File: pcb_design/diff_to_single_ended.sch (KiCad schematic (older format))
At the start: 10 parts, among them U14 OPA2376AID

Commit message: Completed some part numbers
Signed-off-by: Marcos Chaparro <mchaparro@paltatech.com>
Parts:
- C65: MFR (none) -> KEMET; MPN (none) -> C0603C101J5GACTU; SPN (none) -> 399-1061-1-ND; SPR (none) -> Digikey
- C72: MFR (none) -> Murata Electronics North America; MPN (none) -> GRM188R71E104KA01D; SPN (none) -> 490-1524-1-ND; SPR (none) -> Digikey

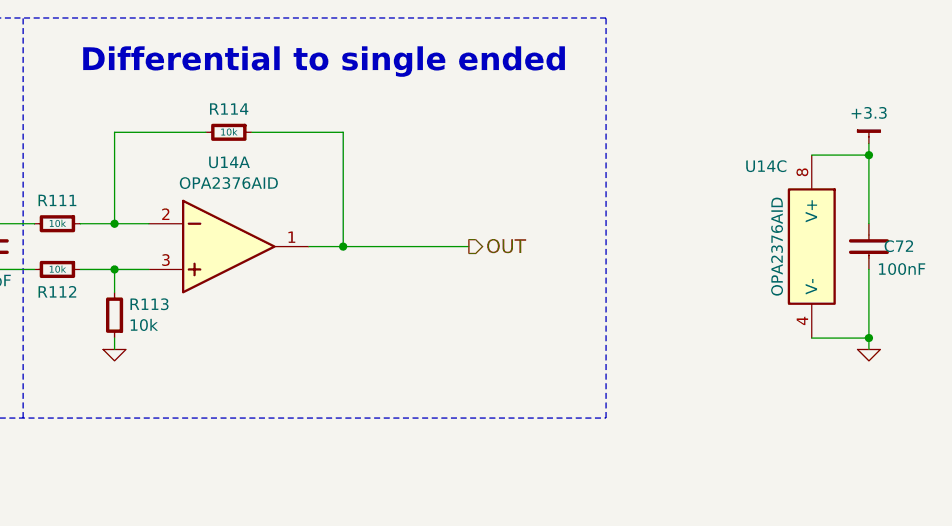
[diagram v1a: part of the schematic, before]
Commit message: Completed part number, manufacturer, etc fields. Simulated analog conditioning
Signed-off-by: Marcos Chaparro <mchaparro@paltatech.com>
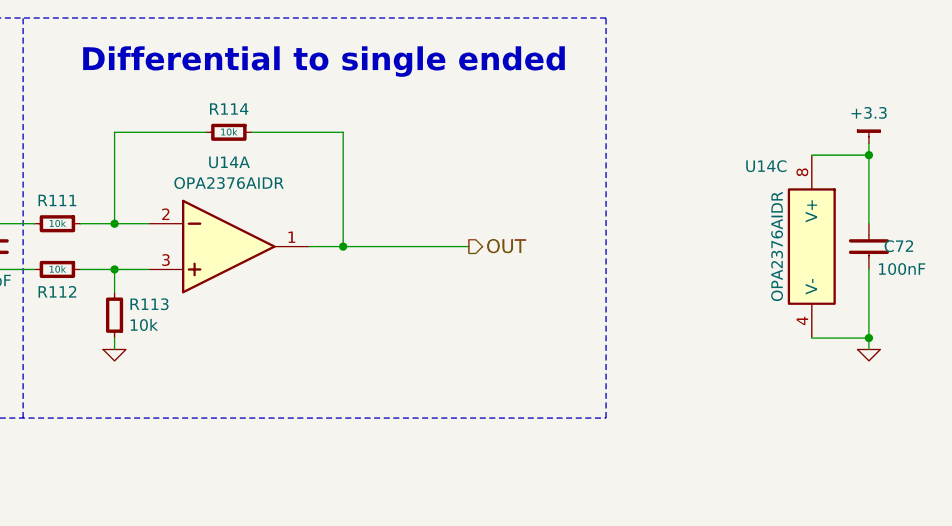
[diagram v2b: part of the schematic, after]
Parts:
- R109, R110: MFR (none) -> Yageo; MPN (none) -> RC0603FR-074K7L; SPN (none) -> 311-4.70KHRCT-ND; SPR (none) -> Digikey
- R111, R112, R113, R114: MFR (none) -> Yageo; MPN (none) -> RC0603FR-0710KL; SPN (none) -> 311-10.0KHRCT-ND; SPR (none) -> Digikey
- R121: MFR (none) -> Yageo; MPN (none) -> RC0603FR-072KL; SPN (none) -> 311-2.00KHRCT-ND; SPR (none) -> Digikey
- U14: value OPA2376AID -> OPA2376AIDR; MFR (none) -> Texas Instruments; MPN (none) -> OPA2376AIDR; SPN (none) -> 296-22564-1-ND; SPR (none) -> Digikey
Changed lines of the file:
@@
 AR Path="/588DB05E/588F2248" Ref="U14" Part="1"
 F 0 "U14" H 6450 4467 50 0000 C CNN
-F 1 "OPA2376AID" H 6450 4376 50 0000 C CNN
+F 1 "OPA2376AIDR" H 6450 4376 50 0000 C CNN
 F 2 "IPC7351-Nominal:SOIC127P600X175-8" H 6400 3850 50 0001 C CNN
-F 3 "" V 6400 4250 60 0000 C CNN
+F 3 "http://www.ti.com/lit/ds/symlink/opa2376.pdf" V 6400 4250 60 0001 C CNN
 F 4 "IC TI OPA2376AID" H 6400 3750 60 0001 C CNN "BOM"
-F 5 "" H 0 0 50 0001 C CNN "MFR"
-F 6 "" H 0 0 50 0001 C CNN "MPN"
-F 7 "" H 0 0 50 0001 C CNN "SPR"
-F 8 "" H 0 0 50 0001 C CNN "SPN"
+F 5 "Texas Instruments" H 0 0 50 0001 C CNN "MFR"
+F 6 "OPA2376AIDR" H 0 0 50 0001 C CNN "MPN"
+F 7 "Digikey" H 0 0 50 0001 C CNN "SPR"
+F 8 "296-22564-1-ND" H 0 0 50 0001 C CNN "SPN"
 F 9 "" H 0 0 50 0001 C CNN "SPURL"
 	1    6400 4100
@@
 F 1 "10k" V 5700 4000 30 0000 C CNN
 F 2 "IPC7351-Nominal:RESC1608X50" H 5700 4000 50 0001 C CNN
-F 3 "" H 5700 4050 60 0000 C CNN
+F 3 "" H 5700 4050 60 0001 C CNN
 F 4 "RES SMD 1k 5% [0603]" H 6450 4550 60 0001 C CNN "BOM"
-F 5 "" H 0 0 50 0001 C CNN "MFR"
-F 6 "" H 0 0 50 0001 C CNN "MPN"
-F 7 "" H 0 0 50 0001 C CNN "SPR"
-F 8 "" H 0 0 50 0001 C CNN "SPN"
+F 5 "Yageo" H 0 0 50 0001 C CNN "MFR"
+F 6 "RC0603FR-0710KL" H 0 0 50 0001 C CNN "MPN"
+F 7 "Digikey" H 0 0 50 0001 C CNN "SPR"
+F 8 "311-10.0KHRCT-ND" H 0 0 50 0001 C CNN "SPN"
 F 9 "" H 0 0 50 0001 C CNN "SPURL"
 	1    5700 4000
@@
 F 1 "10k" V 5700 4200 30 0000 C CNN
 F 2 "IPC7351-Nominal:RESC1608X50" H 5700 4200 50 0001 C CNN
-F 3 "" H 5700 4250 60 0000 C CNN
+F 3 "" H 5700 4250 60 0001 C CNN
 F 4 "RES SMD 1k 5% [0603]" H 6450 4750 60 0001 C CNN "BOM"
-F 5 "" H 0 0 50 0001 C CNN "MFR"
-F 6 "" H 0 0 50 0001 C CNN "MPN"
-F 7 "" H 0 0 50 0001 C CNN "SPR"
-F 8 "" H 0 0 50 0001 C CNN "SPN"
+F 5 "Yageo" H 0 0 50 0001 C CNN "MFR"
+F 6 "RC0603FR-0710KL" H 0 0 50 0001 C CNN "MPN"
+F 7 "Digikey" H 0 0 50 0001 C CNN "SPR"
+F 8 "311-10.0KHRCT-ND" H 0 0 50 0001 C CNN "SPN"
 F 9 "" H 0 0 50 0001 C CNN "SPURL"
 	1    5700 4200
@@
 F 1 "10k" V 6450 3600 30 0000 C CNN
 F 2 "IPC7351-Nominal:RESC1608X50" H 6450 3600 50 0001 C CNN
-F 3 "" H 6450 3650 60 0000 C CNN
+F 3 "" H 6450 3650 60 0001 C CNN
 F 4 "RES SMD 1k 5% [0603]" H 7200 4150 60 0001 C CNN "BOM"
-F 5 "" H 0 0 50 0001 C CNN "MFR"
-F 6 "" H 0 0 50 0001 C CNN "MPN"
-F 7 "" H 0 0 50 0001 C CNN "SPR"
-F 8 "" H 0 0 50 0001 C CNN "SPN"
+F 5 "Yageo" H 0 0 50 0001 C CNN "MFR"
+F 6 "RC0603FR-0710KL" H 0 0 50 0001 C CNN "MPN"
+F 7 "Digikey" H 0 0 50 0001 C CNN "SPR"
+F 8 "311-10.0KHRCT-ND" H 0 0 50 0001 C CNN "SPN"
 F 9 "" H 0 0 50 0001 C CNN "SPURL"
 	1    6450 3600
@@
 F 1 "10k" H 5887 4445 50 0000 R CNN
 F 2 "IPC7351-Nominal:RESC1608X50" H 5950 4400 50 0001 C CNN
-F 3 "" H 5950 4450 60 0000 C CNN
+F 3 "" H 5950 4450 60 0001 C CNN
 F 4 "RES SMD 1k 5% [0603]" H 6700 4950 60 0001 C CNN "BOM"
-F 5 "" H 0 0 50 0001 C CNN "MFR"
-F 6 "" H 0 0 50 0001 C CNN "MPN"
-F 7 "" H 0 0 50 0001 C CNN "SPR"
-F 8 "" H 0 0 50 0001 C CNN "SPN"
+F 5 "Yageo" H 0 0 50 0001 C CNN "MFR"
+F 6 "RC0603FR-0710KL" H 0 0 50 0001 C CNN "MPN"
+F 7 "Digikey" H 0 0 50 0001 C CNN "SPR"
+F 8 "311-10.0KHRCT-ND" H 0 0 50 0001 C CNN "SPN"
 F 9 "" H 0 0 50 0001 C CNN "SPURL"
 	1    5950 4400
@@
 F 1 "4.7k" V 5100 4000 30 0000 C CNN
 F 2 "IPC7351-Nominal:RESC1608X50" H 5100 4000 50 0001 C CNN
-F 3 "" H 5100 4050 60 0000 C CNN
+F 3 "" H 5100 4050 60 0001 C CNN
 F 4 "RES SMD 1k 5% [0603]" H 5850 4550 60 0001 C CNN "BOM"
-F 5 "" H 0 0 50 0001 C CNN "MFR"
-F 6 "" H 0 0 50 0001 C CNN "MPN"
-F 7 "" H 0 0 50 0001 C CNN "SPR"
-F 8 "" H 0 0 50 0001 C CNN "SPN"
+F 5 "Yageo" H 0 0 50 0001 C CNN "MFR"
+F 6 "RC0603FR-074K7L" H 0 0 50 0001 C CNN "MPN"
+F 7 "Digikey" H 0 0 50 0001 C CNN "SPR"
+F 8 "311-4.70KHRCT-ND" H 0 0 50 0001 C CNN "SPN"
 F 9 "" H 0 0 50 0001 C CNN "SPURL"
 	1    5100 4000
@@
 F 1 "4.7k" V 5100 4200 30 0000 C CNN
 F 2 "IPC7351-Nominal:RESC1608X50" H 5100 4200 50 0001 C CNN
-F 3 "" H 5100 4250 60 0000 C CNN
+F 3 "" H 5100 4250 60 0001 C CNN
 F 4 "RES SMD 1k 5% [0603]" H 5850 4750 60 0001 C CNN "BOM"
-F 5 "" H 0 0 50 0001 C CNN "MFR"
-F 6 "" H 0 0 50 0001 C CNN "MPN"
-F 7 "" H 0 0 50 0001 C CNN "SPR"
-F 8 "" H 0 0 50 0001 C CNN "SPN"
+F 5 "Yageo" H 0 0 50 0001 C CNN "MFR"
+F 6 "RC0603FR-074K7L" H 0 0 50 0001 C CNN "MPN"
+F 7 "Digikey" H 0 0 50 0001 C CNN "SPR"
+F 8 "311-4.70KHRCT-ND" H 0 0 50 0001 C CNN "SPN"
 F 9 "" H 0 0 50 0001 C CNN "SPURL"
 	1    5100 4200
@@
 AR Path="/588DB05E/588F2CD6" Ref="U14" Part="3"
 F 0 "U14" H 8800 4450 50 0000 C CNN
-F 1 "OPA2376AID" V 8850 4100 50 0000 C CNN
+F 1 "OPA2376AIDR" V 8850 4100 50 0000 C CNN
 F 2 "IPC7351-Nominal:SOIC127P600X175-8" H 9000 3850 50 0001 C CNN
-F 3 "" V 9000 4250 60 0000 C CNN
+F 3 "http://www.ti.com/lit/ds/symlink/opa2376.pdf" V 9000 4250 60 0001 C CNN
 F 4 "IC TI OPA2376AID" H 9000 3750 60 0001 C CNN "BOM"
-F 5 "" H 0 0 50 0001 C CNN "MFR"
-F 6 "" H 0 0 50 0001 C CNN "MPN"
-F 7 "" H 0 0 50 0001 C CNN "SPR"
-F 8 "" H 0 0 50 0001 C CNN "SPN"
+F 5 "Texas Instruments" H 0 0 50 0001 C CNN "MFR"
+F 6 "OPA2376AIDR" H 0 0 50 0001 C CNN "MPN"
+F 7 "Digikey" H 0 0 50 0001 C CNN "SPR"
+F 8 "296-22564-1-ND" H 0 0 50 0001 C CNN "SPN"
 F 9 "" H 0 0 50 0001 C CNN "SPURL"
 	3    9000 4100
@@
 F 1 "2k" V 4800 4100 30 0000 C CNN
 F 2 "IPC7351-Nominal:RESC1608X50" H 4800 4100 50 0001 C CNN
-F 3 "" H 4800 4150 60 0000 C CNN
+F 3 "" H 4800 4150 60 0001 C CNN
 F 4 "RES SMD 1k 5% [0603]" H 5550 4650 60 0001 C CNN "BOM"
-F 5 "" H 0 0 50 0001 C CNN "MFR"
-F 6 "" H 0 0 50 0001 C CNN "MPN"
-F 7 "" H 0 0 50 0001 C CNN "SPR"
-F 8 "" H 0 0 50 0001 C CNN "SPN"
+F 5 "Yageo" H 0 0 50 0001 C CNN "MFR"
+F 6 "RC0603FR-072KL" H 0 0 50 0001 C CNN "MPN"
+F 7 "Digikey" H 0 0 50 0001 C CNN "SPR"
+F 8 "311-2.00KHRCT-ND" H 0 0 50 0001 C CNN "SPN"
 F 9 "" H 0 0 50 0001 C CNN "SPURL"
 	1    4800 4100

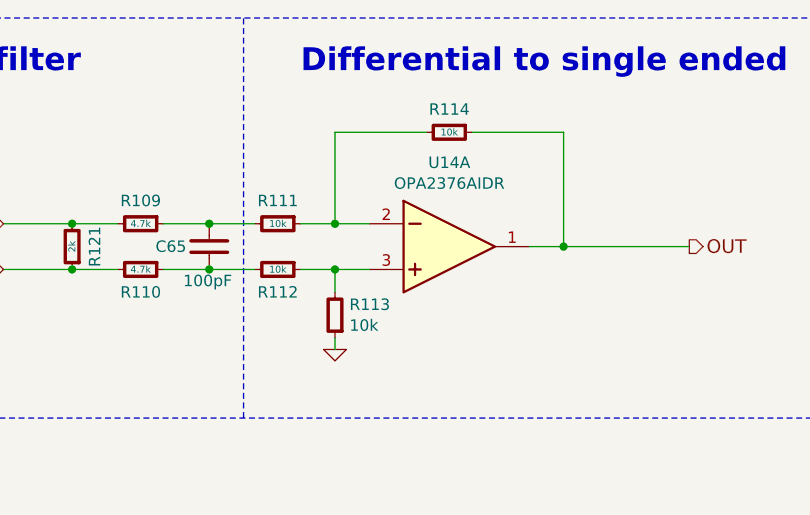
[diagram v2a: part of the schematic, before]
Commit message: Corrected phase current gain. More 3d models
Signed-off-by: Marcos Chaparro <mchaparro@paltatech.com>
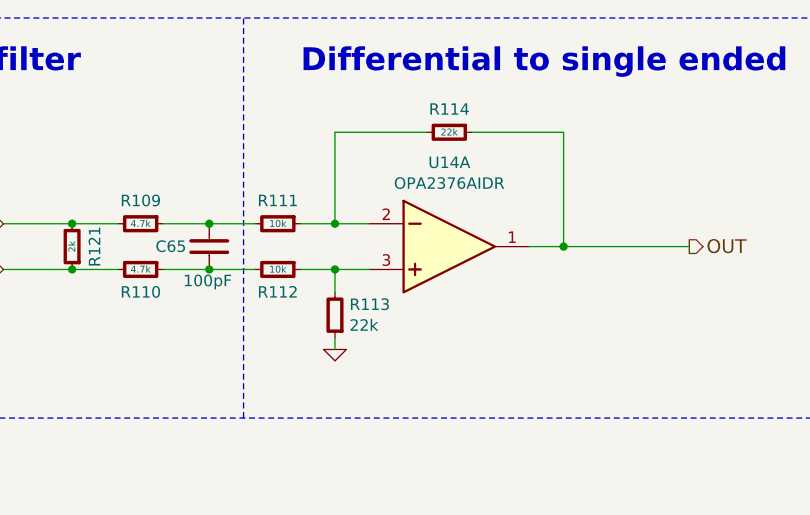
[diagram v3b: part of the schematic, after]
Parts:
- R113, R114: value 10k -> 22k

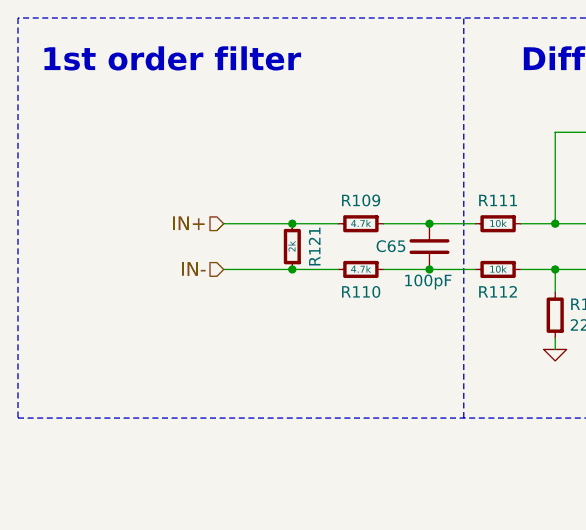
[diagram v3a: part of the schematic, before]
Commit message: Fix inverted diff signals
Signed-off-by: Marcos Chaparro <mchaparro@paltatech.com>
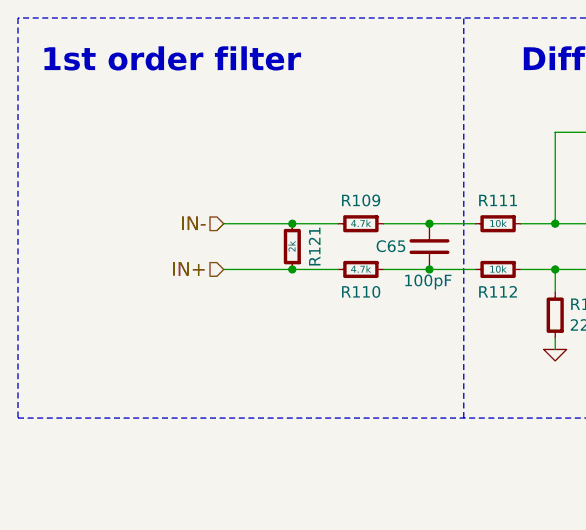
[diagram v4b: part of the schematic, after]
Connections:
- net IN+: now also R110.2, R121.1; no longer R109.2, R121.2
- net IN-: now also R109.2, R121.2; no longer R110.2, R121.1
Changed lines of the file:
@@
 $Descr A4 11693 8268
 encoding utf-8
-Sheet 13 14
+Sheet 11 14
 Title "Differential to single ended"
 Date "2017-02-22"
@@
 EndData
 $EndBitmap
+Text HLabel 4500 4200 0    60   Input ~ 0
+IN+
 Text HLabel 4500 4000 0    60   Input ~ 0
-IN+
-Text HLabel 4500 4200 0    60   Input ~ 0
 IN-
 Text HLabel 7500 4100 2    60   Output ~ 0

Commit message: Added RC filter to FAULT line to prevent noise triggering it
Signed-off-by: Marcos Chaparro <mchaparro@paltatech.com>
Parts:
- C72: BOM CAP MLCC 100pF C0G 50V 5% [0603] -> CAP MLCC 100nF C0G 50V 5% [0603]
- R113, R114: MPN RC0603FR-0710KL -> RC0603FR-0722KL; SPN 311-10.0KHRCT-ND -> 311-22.0KHRCT-ND
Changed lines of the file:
@@
 F 4 "RES SMD 1k 5% [0603]" H 7200 4150 60  0001 C CNN "BOM"
 F 5 "Yageo" H 0   0   50  0001 C CNN "MFR"
-F 6 "RC0603FR-0710KL" H 0   0   50  0001 C CNN "MPN"
+F 6 "RC0603FR-0722KL" H 0   0   50  0001 C CNN "MPN"
 F 7 "Digikey" H 0   0   50  0001 C CNN "SPR"
-F 8 "311-10.0KHRCT-ND" H 0   0   50  0001 C CNN "SPN"
+F 8 "311-22.0KHRCT-ND" H 0   0   50  0001 C CNN "SPN"
 F 9 "" H 0   0   50  0001 C CNN "SPURL"
 	1    6450 3600
@@
 F 4 "RES SMD 1k 5% [0603]" H 6700 4950 60  0001 C CNN "BOM"
 F 5 "Yageo" H 0   0   50  0001 C CNN "MFR"
-F 6 "RC0603FR-0710KL" H 0   0   50  0001 C CNN "MPN"
+F 6 "RC0603FR-0722KL" H 0   0   50  0001 C CNN "MPN"
 F 7 "Digikey" H 0   0   50  0001 C CNN "SPR"
-F 8 "311-10.0KHRCT-ND" H 0   0   50  0001 C CNN "SPN"
+F 8 "311-22.0KHRCT-ND" H 0   0   50  0001 C CNN "SPN"
 F 9 "" H 0   0   50  0001 C CNN "SPURL"
 	1    5950 4400
@@
 F 2 "IPC7351-Nominal:CAPC1608X55" H 9250 4100 50  0001 C CNN
 F 3 "http://www.murata.com/~/media/webrenewal/support/library/catalog/products/capacitor/mlcc/c02e.ashx" H 9240 4075 60  0001 C CNN
-F 4 "CAP MLCC 100pF C0G 50V 5% [0603]" H 10050 4650 60  0001 C CNN "BOM"
+F 4 "CAP MLCC 100nF C0G 50V 5% [0603]" H 10050 4650 60  0001 C CNN "BOM"
 F 5 "Murata Electronics North America" H 0   0   50  0001 C CNN "MFR"
 F 6 "GRM188R71E104KA01D" H 0   0   50  0001 C CNN "MPN"
